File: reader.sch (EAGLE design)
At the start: 12 parts, among them J1 RJ11-6PTH

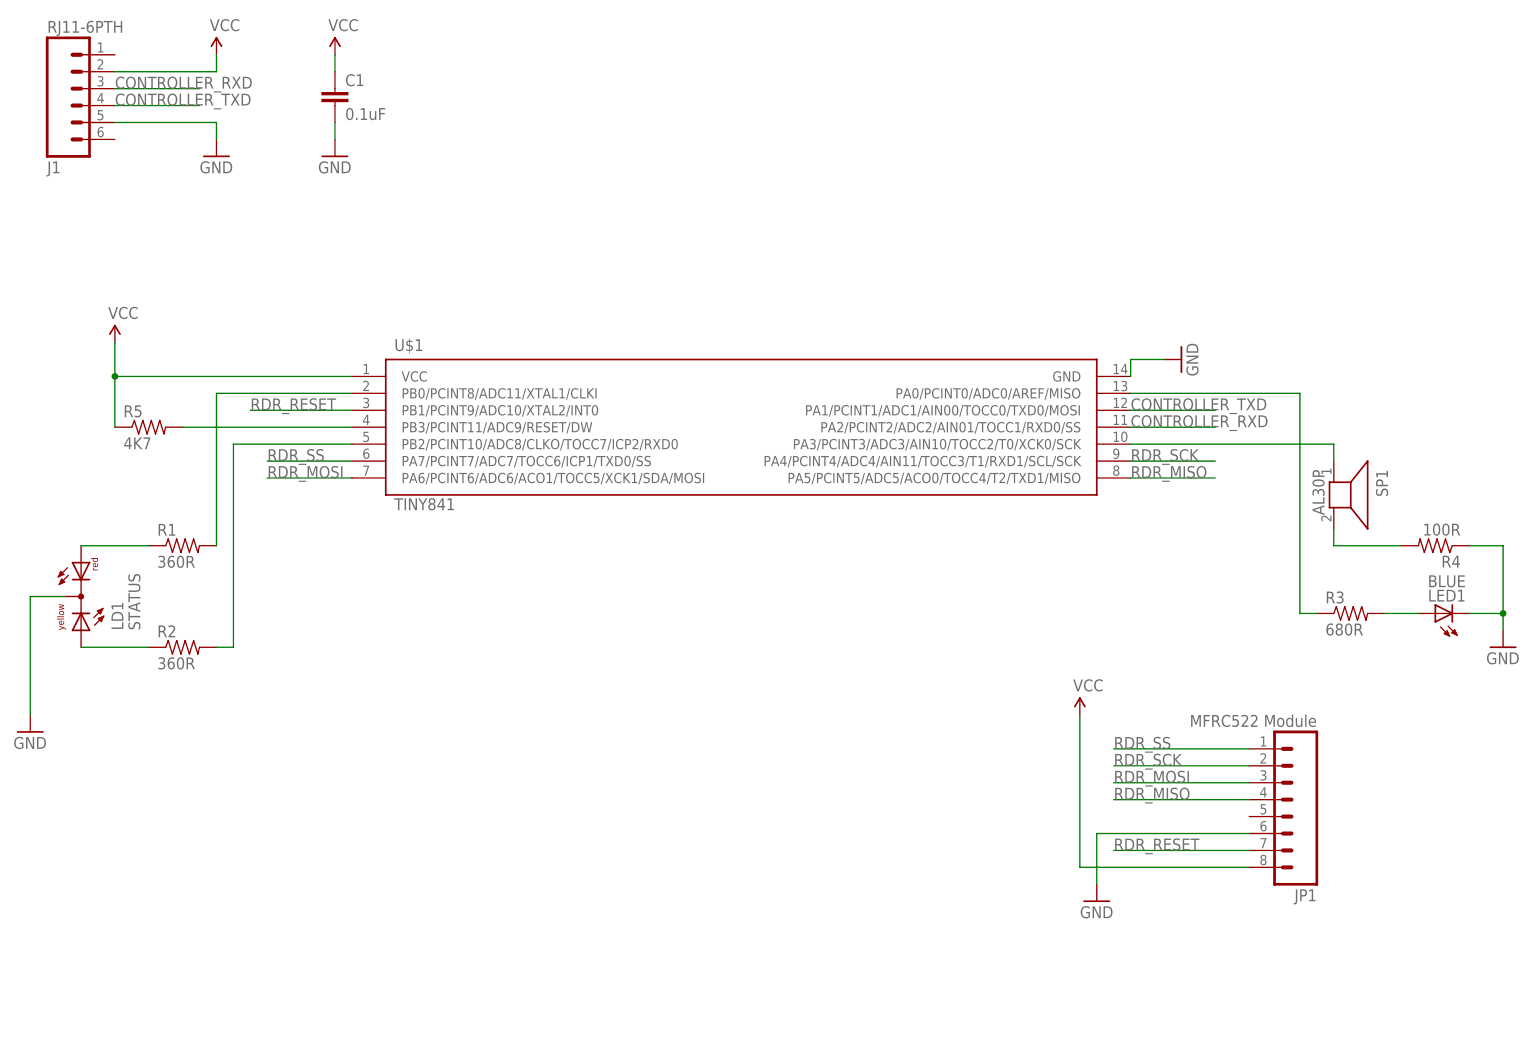
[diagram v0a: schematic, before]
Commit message: Connect speaker directly to the main bus, connect rst
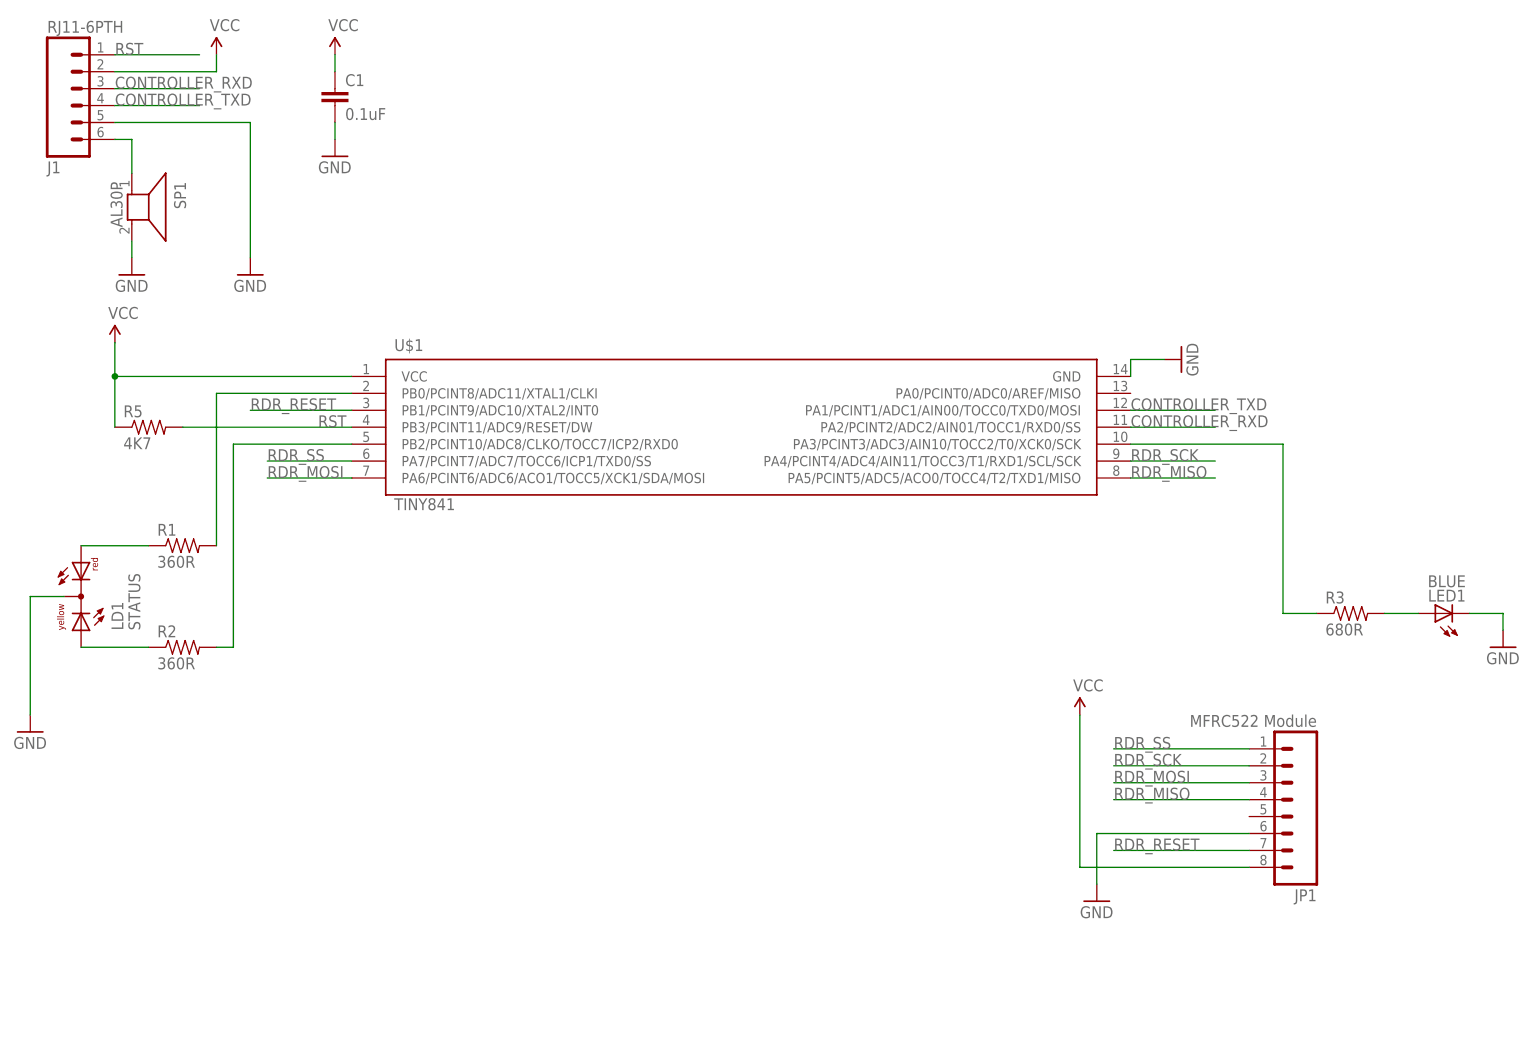
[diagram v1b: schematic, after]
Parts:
- removed R4: 100R, SparkFun-Passives:RESISTOR0805-RES
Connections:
- removed net N$7: R3.1, U$1.PA0/PCINT0/ADC0/AREF/MISO
- removed net N$9: SP1.1, U$1.PA3/PCINT3/ADC3/AIN10/TOCC2/T0/XCK0/SCK
- new net RST: J1.1, R5.2, U$1.PB3/PCINT11/ADC9/RESET/DW
- net GND: now also SP1.2; no longer R4.1
- net N$1: now also J1.6, SP1.1; no longer R4.2, SP1.2
- net N$8: now also R3.1, U$1.PA3/PCINT3/ADC3/AIN10/TOCC2/T0/XCK0/SCK; no longer R5.2, U$1.PB3/PCINT11/ADC9/RESET/DW
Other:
- moved on the sheet: SP1
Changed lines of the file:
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@@
 <part name="GND4" library="SparkFun-Aesthetics" deviceset="GND" device=""/>
 <part name="SP1" library="buzzer" deviceset="AL30P" device=""/>
-<part name="R4" library="SparkFun-Passives" deviceset="RESISTOR" device="0805-RES" value="100R"/>
 <part name="LD1" library="led" deviceset="DUOLED-RY-C" device="" value="STATUS"/>
 <part name="J1" library="SparkFun-Connectors" deviceset="RJ11-6" device="PTH"/>
@@
 <part name="SUPPLY4" library="SparkFun-Aesthetics" deviceset="VCC" device=""/>
 <part name="R5" library="SparkFun-Passives" deviceset="RESISTOR" device="0805-RES" value="4K7"/>
+<part name="GND7" library="SparkFun-Aesthetics" deviceset="GND" device=""/>
 </parts>
 <sheets>
@@
 <instance part="R3" gate="G$1" x="88.9" y="-2.54"/>
 <instance part="GND4" gate="1" x="111.76" y="-7.62"/>
-<instance part="SP1" gate="G$1" x="86.36" y="15.24" rot="R270"/>
-<instance part="R4" gate="G$1" x="101.6" y="7.62" rot="R180"/>
+<instance part="SP1" gate="G$1" x="-93.98" y="58.42" rot="R270"/>
 <instance part="LD1" gate="G$1" x="-101.6" y="0"/>
 <instance part="J1" gate="G$1" x="-101.6" y="76.2" rot="MR180"/>
 <instance part="SUPPLY3" gate="G$1" x="-81.28" y="81.28"/>
-<instance part="GND5" gate="1" x="-81.28" y="66.04"/>
+<instance part="GND5" gate="1" x="-76.2" y="48.26"/>
 <instance part="JP1" gate="G$1" x="78.74" y="-30.48" rot="R180"/>
 <instance part="GND6" gate="1" x="50.8" y="-45.72"/>
 <instance part="SUPPLY4" gate="G$1" x="48.26" y="-17.78"/>
 <instance part="R5" gate="G$1" x="-91.44" y="25.4"/>
+<instance part="GND7" gate="1" x="-93.98" y="48.26"/>
 </instances>
 <busses>
@@
 <pinref part="LED1" gate="G$1" pin="C"/>
 <wire x1="111.76" y1="-2.54" x2="106.68" y2="-2.54" width="0.1524" layer="91"/>
-<pinref part="R4" gate="G$1" pin="1"/>
-<wire x1="106.68" y1="7.62" x2="111.76" y2="7.62" width="0.1524" layer="91"/>
-<wire x1="111.76" y1="7.62" x2="111.76" y2="-2.54" width="0.1524" layer="91"/>
-<junction x="111.76" y="-2.54"/>
 </segment>
 <segment>
 <pinref part="J1" gate="G$1" pin="5"/>
-<wire x1="-96.52" y1="71.12" x2="-81.28" y2="71.12" width="0.1524" layer="91"/>
+<wire x1="-96.52" y1="71.12" x2="-76.2" y2="71.12" width="0.1524" layer="91"/>
 <pinref part="GND5" gate="1" pin="GND"/>
-<wire x1="-81.28" y1="71.12" x2="-81.28" y2="68.58" width="0.1524" layer="91"/>
+<wire x1="-76.2" y1="71.12" x2="-76.2" y2="50.8" width="0.1524" layer="91"/>
 </segment>
 <segment>
@@
 <wire x1="50.8" y1="-35.56" x2="50.8" y2="-43.18" width="0.1524" layer="91"/>
 <pinref part="GND6" gate="1" pin="GND"/>
+</segment>
+<segment>
+<pinref part="GND7" gate="1" pin="GND"/>
+<pinref part="SP1" gate="G$1" pin="2"/>
+<wire x1="-93.98" y1="50.8" x2="-93.98" y2="53.34" width="0.1524" layer="91"/>
 </segment>
 </net>
@@
 </segment>
 </net>
-<net name="N$7" class="0">
-<segment>
-<pinref part="R3" gate="G$1" pin="1"/>
-<wire x1="83.82" y1="-2.54" x2="81.28" y2="-2.54" width="0.1524" layer="91"/>
-<wire x1="81.28" y1="-2.54" x2="81.28" y2="30.48" width="0.1524" layer="91"/>
-<pinref part="U$1" gate="G$1" pin="PA0/PCINT0/ADC0/AREF/MISO"/>
-<wire x1="81.28" y1="30.48" x2="55.88" y2="30.48" width="0.1524" layer="91"/>
-</segment>
-</net>
-<net name="N$1" class="0">
-<segment>
-<pinref part="SP1" gate="G$1" pin="2"/>
-<wire x1="86.36" y1="10.16" x2="86.36" y2="7.62" width="0.1524" layer="91"/>
-<pinref part="R4" gate="G$1" pin="2"/>
-<wire x1="86.36" y1="7.62" x2="96.52" y2="7.62" width="0.1524" layer="91"/>
-</segment>
-</net>
-<net name="N$9" class="0">
-<segment>
-<pinref part="SP1" gate="G$1" pin="1"/>
-<wire x1="86.36" y1="20.32" x2="86.36" y2="22.86" width="0.1524" layer="91"/>
-<pinref part="U$1" gate="G$1" pin="PA3/PCINT3/ADC3/AIN10/TOCC2/T0/XCK0/SCK"/>
-<wire x1="86.36" y1="22.86" x2="55.88" y2="22.86" width="0.1524" layer="91"/>
-</segment>
-</net>
 <net name="CONTROLLER_RXD" class="0">
 <segment>
@@
 </segment>
 </net>
-<net name="N$8" class="0">
+<net name="RST" class="0">
+<segment>
+<pinref part="J1" gate="G$1" pin="1"/>
+<wire x1="-96.52" y1="81.28" x2="-83.82" y2="81.28" width="0.1524" layer="91"/>
+<label x="-96.52" y="81.28" size="1.778" layer="95"/>
+</segment>
 <segment>
 <pinref part="U$1" gate="G$1" pin="PB3/PCINT11/ADC9/RESET/DW"/>
 <wire x1="-60.96" y1="25.4" x2="-86.36" y2="25.4" width="0.1524" layer="91"/>
 <pinref part="R5" gate="G$1" pin="2"/>
-</segment>
-</net>
+<label x="-66.04" y="25.4" size="1.778" layer="95"/>
+</segment>
+</net>
+<net name="N$8" class="0">
+<segment>
+<pinref part="R3" gate="G$1" pin="1"/>
+<wire x1="83.82" y1="-2.54" x2="78.74" y2="-2.54" width="0.1524" layer="91"/>
+<wire x1="78.74" y1="-2.54" x2="78.74" y2="22.86" width="0.1524" layer="91"/>
+<pinref part="U$1" gate="G$1" pin="PA3/PCINT3/ADC3/AIN10/TOCC2/T0/XCK0/SCK"/>
+<wire x1="78.74" y1="22.86" x2="55.88" y2="22.86" width="0.1524" layer="91"/>
+</segment>
+</net>
+<net name="N$1" class="0">
+<segment>
+<pinref part="J1" gate="G$1" pin="6"/>
+<pinref part="SP1" gate="G$1" pin="1"/>
+<wire x1="-96.52" y1="68.58" x2="-93.98" y2="68.58" width="0.1524" layer="91"/>
+<wire x1="-93.98" y1="68.58" x2="-93.98" y2="63.5" width="0.1524" layer="91"/>
+</segment>
+</net>

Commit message: Add option for sound source selection
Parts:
- added JP2, JP3: (no value), SparkFun-Retired:JUMPER-2PTH
- added R4: 66R, SparkFun-Passives:RESISTOR0805-RES
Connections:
- net N$4 renamed RED_LED
- net N$5 renamed GREEN_LED
- net N$8 renamed BLUE_LED
- new net EXT_SPEAKER: J1.6, JP2.1
- new net N$9: JP3.1, R4.2
- new net SPEAKER: R4.1, U$1.PA0/PCINT0/ADC0/AREF/MISO
- net N$1: now also JP2.2, JP3.2; no longer J1.6
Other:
- note added: "sound source select"
- moved on the sheet: C1, SP1
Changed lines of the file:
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@@
 <part name="R5" library="SparkFun-Passives" deviceset="RESISTOR" device="0805-RES" value="4K7"/>
 <part name="GND7" library="SparkFun-Aesthetics" deviceset="GND" device=""/>
+<part name="JP2" library="SparkFun-Retired" deviceset="JUMPER-2" device="PTH"/>
+<part name="JP3" library="SparkFun-Retired" deviceset="JUMPER-2" device="PTH"/>
+<part name="R4" library="SparkFun-Passives" deviceset="RESISTOR" device="0805-RES" value="66R"/>
 </parts>
 <sheets>
 <sheet>
 <plain>
+<text x="-24.638" y="42.672" size="1.778" layer="91">sound
+source
+select</text>
 </plain>
 <instances>
@@
 <instance part="SUPPLY1" gate="G$1" x="-96.52" y="38.1"/>
 <instance part="GND1" gate="1" x="63.5" y="35.56" rot="R90"/>
-<instance part="C1" gate="G$1" x="-63.5" y="73.66"/>
-<instance part="SUPPLY2" gate="G$1" x="-63.5" y="81.28"/>
-<instance part="GND2" gate="1" x="-63.5" y="66.04"/>
+<instance part="C1" gate="G$1" x="-60.96" y="73.66"/>
+<instance part="SUPPLY2" gate="G$1" x="-60.96" y="81.28"/>
+<instance part="GND2" gate="1" x="-60.96" y="65.786"/>
 <instance part="GND3" gate="1" x="-109.22" y="-20.32"/>
 <instance part="R1" gate="G$1" x="-86.36" y="7.62"/>
@@
 <instance part="R3" gate="G$1" x="88.9" y="-2.54"/>
 <instance part="GND4" gate="1" x="111.76" y="-7.62"/>
-<instance part="SP1" gate="G$1" x="-93.98" y="58.42" rot="R270"/>
+<instance part="SP1" gate="G$1" x="-2.54" y="63.5" rot="R270"/>
 <instance part="LD1" gate="G$1" x="-101.6" y="0"/>
 <instance part="J1" gate="G$1" x="-101.6" y="76.2" rot="MR180"/>
@@
 <instance part="SUPPLY4" gate="G$1" x="48.26" y="-17.78"/>
 <instance part="R5" gate="G$1" x="-91.44" y="25.4"/>
-<instance part="GND7" gate="1" x="-93.98" y="48.26"/>
+<instance part="GND7" gate="1" x="-2.54" y="53.34"/>
+<instance part="JP2" gate="A" x="-22.86" y="60.96"/>
+<instance part="JP3" gate="A" x="-22.86" y="53.34"/>
+<instance part="R4" gate="G$1" x="-33.02" y="50.8"/>
 </instances>
 <busses>
@@
 <pinref part="SUPPLY2" gate="G$1" pin="VCC"/>
 <pinref part="C1" gate="G$1" pin="1"/>
-<wire x1="-63.5" y1="81.28" x2="-63.5" y2="78.74" width="0.1524" layer="91"/>
+<wire x1="-60.96" y1="81.28" x2="-60.96" y2="78.74" width="0.1524" layer="91"/>
 </segment>
 <segment>
@@
 <pinref part="C1" gate="G$1" pin="2"/>
 <pinref part="GND2" gate="1" pin="GND"/>
-<wire x1="-63.5" y1="71.12" x2="-63.5" y2="68.58" width="0.1524" layer="91"/>
+<wire x1="-60.96" y1="71.12" x2="-60.96" y2="68.326" width="0.1524" layer="91"/>
 </segment>
 <segment>
@@
 <pinref part="GND7" gate="1" pin="GND"/>
 <pinref part="SP1" gate="G$1" pin="2"/>
-<wire x1="-93.98" y1="50.8" x2="-93.98" y2="53.34" width="0.1524" layer="91"/>
+<wire x1="-2.54" y1="55.88" x2="-2.54" y2="58.42" width="0.1524" layer="91"/>
 </segment>
 </net>
@@
 </segment>
 </net>
-<net name="N$4" class="0">
+<net name="RED_LED" class="0">
 <segment>
 <pinref part="R1" gate="G$1" pin="2"/>
@@
 </segment>
 </net>
-<net name="N$5" class="0">
+<net name="GREEN_LED" class="0">
 <segment>
 <pinref part="R2" gate="G$1" pin="2"/>
@@
 </segment>
 </net>
-<net name="N$8" class="0">
+<net name="BLUE_LED" class="0">
 <segment>
 <pinref part="R3" gate="G$1" pin="1"/>
@@
 <net name="N$1" class="0">
 <segment>
+<wire x1="-15.24" y1="50.8" x2="-15.24" y2="58.42" width="0.1524" layer="91"/>
+<pinref part="JP3" gate="A" pin="2"/>
+<wire x1="-15.24" y1="58.42" x2="-15.24" y2="68.58" width="0.1524" layer="91"/>
+<wire x1="-15.24" y1="50.8" x2="-20.32" y2="50.8" width="0.1524" layer="91"/>
+<pinref part="SP1" gate="G$1" pin="1"/>
+<wire x1="-15.24" y1="68.58" x2="-2.54" y2="68.58" width="0.1524" layer="91"/>
+<pinref part="JP2" gate="A" pin="2"/>
+<wire x1="-20.32" y1="58.42" x2="-15.24" y2="58.42" width="0.1524" layer="91"/>
+<junction x="-15.24" y="58.42"/>
+</segment>
+</net>
+<net name="EXT_SPEAKER" class="0">
+<segment>
+<pinref part="JP2" gate="A" pin="1"/>
 <pinref part="J1" gate="G$1" pin="6"/>
-<pinref part="SP1" gate="G$1" pin="1"/>
-<wire x1="-96.52" y1="68.58" x2="-93.98" y2="68.58" width="0.1524" layer="91"/>
-<wire x1="-93.98" y1="68.58" x2="-93.98" y2="63.5" width="0.1524" layer="91"/>
+<wire x1="-22.86" y1="58.42" x2="-96.52" y2="58.42" width="0.1524" layer="91"/>
+<wire x1="-96.52" y1="58.42" x2="-96.52" y2="68.58" width="0.1524" layer="91"/>
+</segment>
+</net>
+<net name="SPEAKER" class="0">
+<segment>
+<pinref part="U$1" gate="G$1" pin="PA0/PCINT0/ADC0/AREF/MISO"/>
+<wire x1="73.66" y1="30.48" x2="55.88" y2="30.48" width="0.1524" layer="91"/>
+<label x="55.88" y="30.48" size="1.778" layer="95"/>
+</segment>
+<segment>
+<pinref part="R4" gate="G$1" pin="1"/>
+<wire x1="-38.1" y1="50.8" x2="-48.26" y2="50.8" width="0.1524" layer="91"/>
+<label x="-48.26" y="50.8" size="1.778" layer="95"/>
+</segment>
+</net>
+<net name="N$9" class="0">
+<segment>
+<pinref part="JP3" gate="A" pin="1"/>
+<wire x1="-22.86" y1="50.8" x2="-27.94" y2="50.8" width="0.1524" layer="91"/>
+<pinref part="R4" gate="G$1" pin="2"/>
 </segment>
 </net>
@@
 </schematic>
 </drawing>
+<compatibility>
+<note version="6.3" minversion="6.2.2" severity="warning">
+Since Version 6.2.2 text objects can contain more than one line,
+which will not be processed correctly with this version.
+</note>
+</compatibility>
 </eagle>
